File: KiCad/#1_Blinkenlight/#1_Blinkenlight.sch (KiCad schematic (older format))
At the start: 17 parts, among them J1 Conn_02x19_Odd_Even

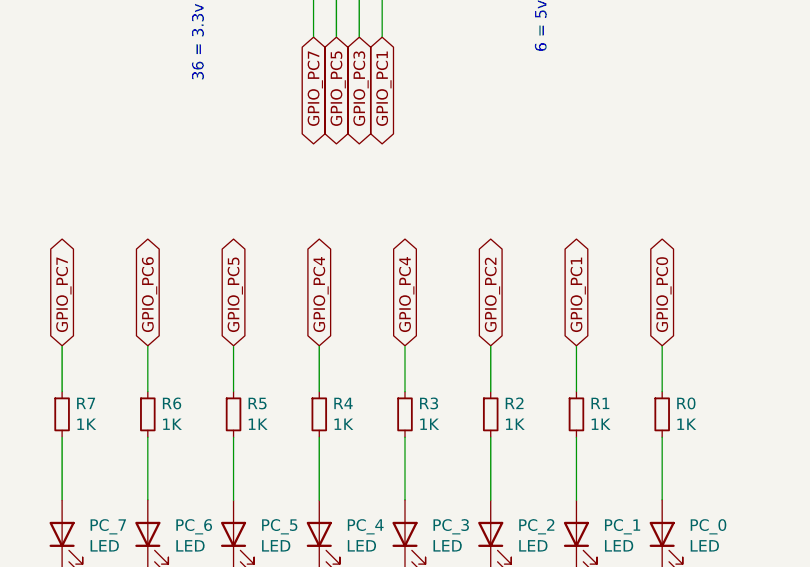
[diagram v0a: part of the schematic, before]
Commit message: Blinkenlight schematic correction
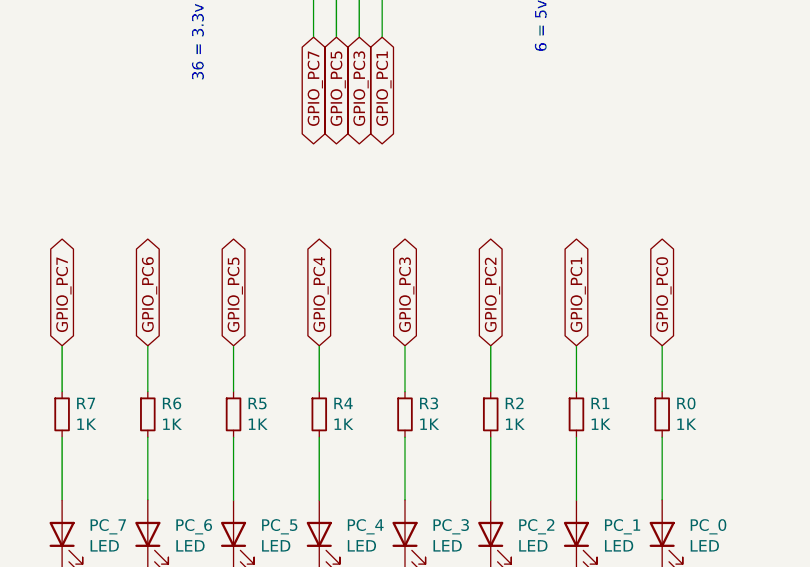
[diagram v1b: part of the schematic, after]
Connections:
- net GPIO_PC3: now also R3.1
- net GPIO_PC4: no longer R3.1
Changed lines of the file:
@@
 Sheet 1 1
 Title "#1 - Blinkenlight"
-Date "2023-04-10"
+Date "2023-05-18"
 Rev "Rev 01"
 Comp "AdamT117 (https://github.com/Kayto/AgonLight_GPIO)"
@@
 GPIO_PC2
 Text GLabel 5875 4225 1    50   BiDi ~ 0
-GPIO_PC4
+GPIO_PC3
 Text GLabel 5500 4225 1    50   BiDi ~ 0
 GPIO_PC4
